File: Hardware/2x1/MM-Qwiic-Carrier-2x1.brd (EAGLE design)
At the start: 109.2 x 34.3 mm, 67 parts, among them J15 MICROMOD-2222-C, J2 QWIIC_RIGHT_ANGLE, U1 MCP73831, U5 AP7361C-33FGEUDFN-8

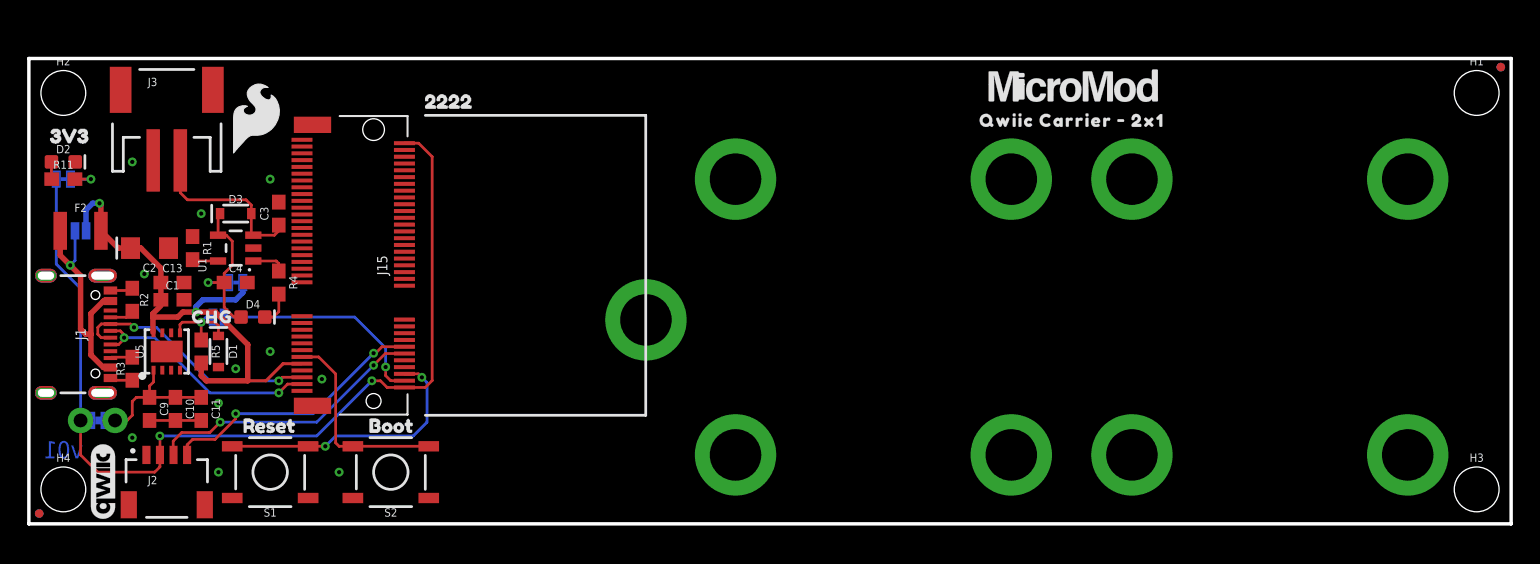
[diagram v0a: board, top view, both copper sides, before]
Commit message: Fix silk screen
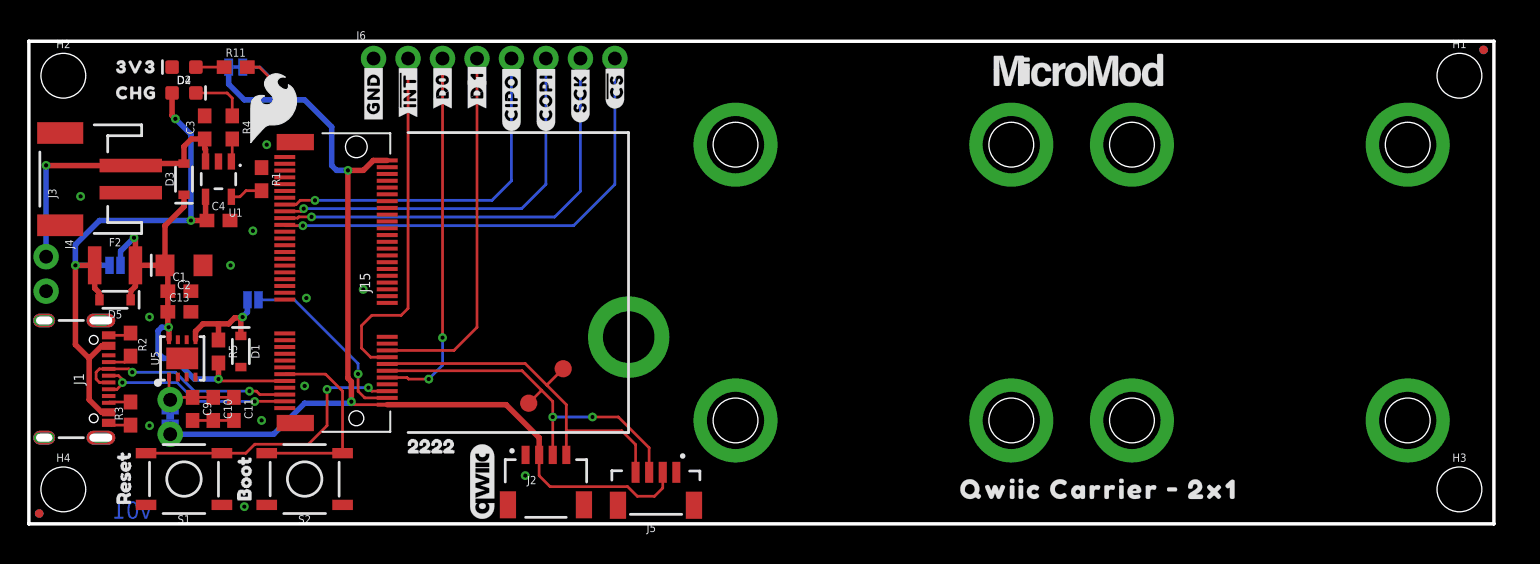
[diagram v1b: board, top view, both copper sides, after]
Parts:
- removed H10, H11, H12, H13, H6, H7, H8, H9: STAND-OFF-REFLOW2.5MM_TALL, SparkFun-Hardware:STAND-OFF-REFLOW-M2.5
- removed JP1: JUMPER-SMT_2_NC_TRACE_SILK, SparkFun-Jumpers:SMT-JUMPER_2_NC_TRACE_SILK
- removed U$10: (no value), output:QWIIC_CARRIER_#_2X10
- added D5: 3A/10V/280mV, SparkFun-DiscreteSemi:SOD-323
- added J4: (no value), SparkFun-Connectors:1X02_NO_SILK
- added J5: Vertical Qwiic Connector, SparkFun-Connectors:JST04_1MM_VERT
- added J6: (no value), SparkFun-Connectors:1X08_NO_SILK
- added TP1, TP2: TEST-POINT3X5, SparkFun-Connectors:PAD.03X.05
- added U$11, U$12: (no value), output:QWIIC_CARRIER_#_2X10
- added U$14: (no value), output:#GND#0
- added U$15, U$16: (no value), output:##INT##0
- added U$17, U$18: (no value), output:#D0#0
- added U$20, U$21: (no value), output:#D#0
- added U$22, U$23: (no value), output:#CIPO#0
- added U$24, U$25: (no value), output:#COPI#0
- added U$26, U$27: (no value), output:#SCK#0
- added U$28, U$29: (no value), output:##CS##0
- added U$3: (no value), output:3V30
- added U$30, U$31: (no value), output:#1#0
- added U$32: QWIIC_BOARD_OUTLINESTANDOFF, SparkFun-Boards:QWIIC_BOARD_MOUNT_SMD_STANDOFFS
- U$1: device buzzard_labels (5):3V31 -> output:#3#3V_EN#0
- U$5: value (none) -> QWIIC_BOARD_OUTLINESTANDOFF; device output:#VIN#0 -> SparkFun-Boards:QWIIC_BOARD_MOUNT_SMD_STANDOFFS
- U$8: device output:#VE#0 -> output:#GND#0
- moved U$5 47.9 mm to (62.2, 17.8), flipped to the top
- moved LOGO2 27.9 mm to (33.4, 3.11)
- moved J2 27.9 mm to (38.1, 5.08)
- moved U$55 25.4 mm to (27.0, 5.72)
- moved U$1 19.3 mm to (15.7, 16.5), flipped to the bottom
- moved U$8 18.7 mm to (25.4, 29.5), flipped to the top, turned to 90 degrees
- moved U$4 17.4 mm to (5.71, 31.8)
- moved D4 17.3 mm to (11.4, 31.8)
- moved JP4 15.1 mm to (15.2, 33.7)
- moved R11 15.1 mm to (15.2, 33.7)
- moved U$6 15.1 mm to (21.0, 33.5)
- moved R4 11.9 mm to (15.0, 29.2)
- moved D2 11.3 mm to (11.4, 33.7), turned to 180 degrees
- moved U$19 10.5 mm to (15.9, 0.76), turned to 90 degrees
- moved U$2 10.4 mm to (6.99, 0.51), turned to 90 degrees
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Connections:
- removed net 5V: C4.1, D3.C, D4.A, JP1.2, U1.4
- removed net I2C_SCL: J15.14, J2.4
- removed net I2C_SDA: J15.12, J2.3
- removed net N$5: C3.1, D3.A, J3.2, U1.3
- new net D0: J15.10, J6.3
- new net D1: J15.18, J6.4
- new net I2C_!INT!: J15.16, J6.2
- new net SCL: J15.14, J2.4, J5.4, TP2.P$1
- new net SDA: J15.12, J2.3, J5.3, TP1.P$1
- new net SPI_!CS!: J15.55, J6.8
- new net SPI_CIPO: J15.61, J6.5
- new net SPI_COPI: J15.59, J6.6
- new net SPI_SCK: J15.57, J6.7
- new net V_BATT: C3.1, D3.A, J3.2, J4.1, U1.3
- net 3.3V: now also J5.2
- net GND: now also J4.2, J5.1, J6.1; no longer H10.1, H11.1, H12.1, H13.1, H6.1, H7.1, H8.1, H9.1
- net N$3: now also D4.C; no longer U1.1
- net N$8: now also U1.1; no longer D4.C
- net VIN: now also D3.C, D5.C; no longer JP1.1
- net V_USB: now also C4.1, D4.A, D5.A, U1.4
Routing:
- net SPI_!CS!: track 0.00 -> 34.9 mm, vias 0 -> 1
- net SPI_SCK: track 0.00 -> 32.4 mm, vias 0 -> 1
- net SPI_COPI: track 0.00 -> 29.3 mm, vias 0 -> 1
- net SDA: track 0.00 -> 28.3 mm, vias 0 -> 2
- net SCL: track 0.00 -> 27.4 mm
- net D0: track 0.00 -> 27.1 mm, vias 0 -> 2
- net D1: track 0.00 -> 27.1 mm
- net SPI_CIPO: track 0.00 -> 26.4 mm, vias 0 -> 1
- net I2C_!INT!: track 0.00 -> 26.2 mm
- net V_USB: track 18.2 -> 44.3 mm, vias 1 -> 3
- net V_BATT: track 0.00 -> 21.7 mm, vias 0 -> 1
- net I2C_SDA: track 20.7 -> 0.00 mm, vias 2 -> 0
- net I2C_SCL: track 20.0 -> 0.00 mm, vias 2 -> 0
- net N$5: track 12.7 -> 0.00 mm
- net 5V: track 12.2 -> 0.00 mm, vias 1 -> 0
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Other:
- board size 109.2 x 34.3 mm -> 108 x 35.6 mm
- board text added: "in"

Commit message: silkscreen
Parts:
- added U$33: (no value), output:#GND#0
- added U$34: QWIIC_BOARD_OUTLINESTANDOFF, SparkFun-Boards:QWIIC_BOARD_MOUNT_SMD_STANDOFFS
- added U$35, U$38: (no value), output:QWIIC_CARRIER_#_2X10
- added U$36, U$37: (no value), buzzard_labels (1):#0
- U$11: device output:QWIIC_CARRIER_#_2X10 -> output:#0
- U$12: device output:QWIIC_CARRIER_#_2X10 -> output:#VBAT#0
- U$32: value QWIIC_BOARD_OUTLINESTANDOFF -> (none); device SparkFun-Boards:QWIIC_BOARD_MOUNT_SMD_STANDOFFS -> output:#0
- moved U$32 84.3 mm to (7.75, 27.8)
- moved U$11 68.2 mm to (1.52, 19.7)
- moved U$12 35.4 mm to (7.37, 19.7)
- moved U$67 15.2 mm to (62.1, 33.4)
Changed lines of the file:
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@@
 <?xml version="1.0" encoding="utf-8"?>
 <!DOCTYPE eagle SYSTEM "eagle.dtd">
-<eagle version="9.5.2">
+<eagle version="9.6.2">
 <drawing>
 <settings>
@@
 <wire x1="44.185" y1="6.731" x2="27.94" y2="6.731" width="0.2032" layer="21"/>
 <text x="36.83" y="-21.59" size="1.778" layer="51" font="vector" ratio="15">Priyanka Makin</text>
-<text x="57.404" y="39.878" size="1.778" layer="47" font="vector" ratio="15">in</text>
-<text x="109.474" y="24.511" size="1.778" layer="47" font="vector" ratio="15" rot="R270">in</text>
-<dimension x1="0" y1="35.56" x2="107.95" y2="35.56" x3="53.975" y3="39.37" textsize="1.778" textratio="15" layer="47" unit="inch"/>
-<dimension x1="107.95" y1="35.56" x2="107.95" y2="1.27" x3="111.76" y3="18.415" textsize="1.778" textratio="15" layer="47" unit="inch"/>
+<dimension x1="0" y1="35.56" x2="80.01" y2="35.56" x3="40.005" y3="39.37" textsize="1.778" textratio="15" layer="47" unit="inch"/>
+<dimension x1="80.01" y1="35.56" x2="80.01" y2="0" x3="83.82" y3="17.78" textsize="1.778" textratio="15" layer="47" unit="inch"/>
+<text x="43.434" y="39.878" size="1.778" layer="47" font="vector" ratio="15">in</text>
+<text x="81.534" y="23.241" size="1.778" layer="47" font="vector" ratio="15" rot="R270">in</text>
+<dimension x1="2.54" y1="33.02" x2="77.47" y2="33.02" x3="40.005" y3="44.45" textsize="1.778" textratio="15" layer="47" unit="inch"/>
+<dimension x1="77.47" y1="33.02" x2="77.47" y2="2.54" x3="88.9" y3="17.78" textsize="1.778" textratio="15" layer="47" unit="inch"/>
+<text x="43.434" y="44.958" size="1.778" layer="47" font="vector" ratio="15">in</text>
+<text x="86.614" y="23.241" size="1.778" layer="47" font="vector" ratio="15" rot="R270">in</text>
 </plain>
 <attributes>
@@
 <element name="LOGO1" library="SparkFun-Aesthetics" package="SFE_LOGO_NAME_FLAME_.2" value="SFE_LOGO_NAME_FLAME.2_INCH" x="31.75" y="21.59" smashed="yes" rot="MR0"/>
 <element name="U$44" library="SparkFun-Aesthetics" package="SFE_LOGO_FLAME_.2" value="" x="18.034" y="30.607" smashed="yes"/>
-<element name="U$67" library="SparkFun-MicroMod" package="MICROMOD_LOGO_.5" value="" x="77.343" y="33.401" smashed="yes"/>
+<element name="U$67" library="SparkFun-MicroMod" package="MICROMOD_LOGO_.5" value="" x="62.103" y="33.401" smashed="yes"/>
 <element name="U$68" library="SparkFun-MicroMod" package="MICROMOD_LOGO_.5" value="" x="31.75" y="19.05" smashed="yes" rot="MR0"/>
 <element name="J2" library="SparkFun-Connectors" package="JST04_1MM_RA" value="QWIIC_RIGHT_ANGLE" x="38.1" y="5.08" smashed="yes">
@@
 </element>
 <element name="U$5" library="SparkFun-Boards" package="QWIIC_BOARD_MOUNT_SMD_STANDOFFS" value="QWIIC_BOARD_OUTLINESTANDOFF" x="62.23" y="17.78" smashed="yes"/>
-<element name="U$11" library="output" package="QWIIC_CARRIER_#_2X10" value="" x="67.564" y="2.54" smashed="yes"/>
-<element name="U$12" library="output" package="QWIIC_CARRIER_#_2X10" value="" x="42.672" y="16.51" smashed="yes" rot="MR0"/>
 <element name="U$3" library="output" package="3V30" value="" x="5.715" y="33.655" smashed="yes"/>
 <element name="U$1" library="output" package="#3#3V_EN#0" value="" x="15.748" y="16.51" smashed="yes" rot="MR0"/>
@@
 <element name="U$30" library="output" package="#1#0" value="" x="33.02" y="32.004" smashed="yes" rot="R90"/>
 <element name="U$31" library="output" package="#1#0" value="" x="33.02" y="32.004" smashed="yes" rot="MR90"/>
-<element name="U$32" library="SparkFun-Boards" package="QWIIC_BOARD_MOUNT_SMD_STANDOFFS" value="QWIIC_BOARD_OUTLINESTANDOFF" x="91.44" y="17.78" smashed="yes"/>
+<element name="U$12" library="output" package="#VBAT#0" value="" x="7.366" y="19.685" smashed="yes" rot="MR0"/>
+<element name="U$33" library="output" package="#GND#0" value="" x="6.096" y="17.145" smashed="yes" rot="MR0"/>
+<element name="U$11" library="output" package="#0" value="" x="1.524" y="19.685" smashed="yes"/>
+<element name="U$32" library="output" package="#0" value="" x="7.747" y="27.813" smashed="yes"/>
+<element name="U$36" library="buzzard_labels (1)" package="#0" value="" x="1.143" y="17.399" smashed="yes"/>
+<element name="U$37" library="buzzard_labels (1)" package="#0" value="" x="7.366" y="23.495" smashed="yes"/>
+<element name="U$34" library="SparkFun-Boards" package="QWIIC_BOARD_MOUNT_SMD_STANDOFFS" value="QWIIC_BOARD_OUTLINESTANDOFF" x="91.44" y="17.78" smashed="yes"/>
+<element name="U$35" library="output" package="QWIIC_CARRIER_#_2X10" value="" x="51.054" y="2.54" smashed="yes"/>
+<element name="U$38" library="output" package="QWIIC_CARRIER_#_2X10" value="" x="42.926" y="16.764" smashed="yes" rot="MR0"/>
 </elements>
 <signals>

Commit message: Update MM-Qwiic-Carrier-2x1.brd
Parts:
- moved U$67 15.2 mm to (77.3, 33.4)
- moved U$35 14.0 mm to (65.0, 2.54)
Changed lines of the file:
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@@
 <?xml version="1.0" encoding="utf-8"?>
 <!DOCTYPE eagle SYSTEM "eagle.dtd">
-<eagle version="9.6.2">
+<eagle version="9.5.2">
 <drawing>
 <settings>
@@
 <wire x1="44.185" y1="6.731" x2="27.94" y2="6.731" width="0.2032" layer="21"/>
 <text x="36.83" y="-21.59" size="1.778" layer="51" font="vector" ratio="15">Priyanka Makin</text>
-<dimension x1="0" y1="35.56" x2="80.01" y2="35.56" x3="40.005" y3="39.37" textsize="1.778" textratio="15" layer="47" unit="inch"/>
-<dimension x1="80.01" y1="35.56" x2="80.01" y2="0" x3="83.82" y3="17.78" textsize="1.778" textratio="15" layer="47" unit="inch"/>
-<text x="43.434" y="39.878" size="1.778" layer="47" font="vector" ratio="15">in</text>
-<text x="81.534" y="23.241" size="1.778" layer="47" font="vector" ratio="15" rot="R270">in</text>
-<dimension x1="2.54" y1="33.02" x2="77.47" y2="33.02" x3="40.005" y3="44.45" textsize="1.778" textratio="15" layer="47" unit="inch"/>
-<dimension x1="77.47" y1="33.02" x2="77.47" y2="2.54" x3="88.9" y3="17.78" textsize="1.778" textratio="15" layer="47" unit="inch"/>
-<text x="43.434" y="44.958" size="1.778" layer="47" font="vector" ratio="15">in</text>
-<text x="86.614" y="23.241" size="1.778" layer="47" font="vector" ratio="15" rot="R270">in</text>
+<text x="57.404" y="39.878" size="1.778" layer="47" font="vector" ratio="15">in</text>
+<text x="110.744" y="23.241" size="1.778" layer="47" font="vector" ratio="15" rot="R270">in</text>
+<text x="57.404" y="43.688" size="1.778" layer="47" font="vector" ratio="15">in</text>
+<text x="114.554" y="23.241" size="1.778" layer="47" font="vector" ratio="15" rot="R270">in</text>
+<dimension x1="0" y1="35.56" x2="107.95" y2="35.56" x3="53.975" y3="43.18" textsize="1.778" textratio="15" layer="47" unit="inch"/>
+<dimension x1="2.54" y1="33.02" x2="105.41" y2="33.02" x3="53.975" y3="39.37" textsize="1.778" textratio="15" layer="47" unit="inch"/>
+<dimension x1="105.41" y1="33.02" x2="105.41" y2="2.54" x3="113.03" y3="17.78" textsize="1.778" textratio="15" layer="47" unit="inch"/>
+<dimension x1="107.95" y1="35.56" x2="107.95" y2="0" x3="116.84" y3="17.78" textsize="1.778" textratio="15" layer="47" unit="inch"/>
 </plain>
 <attributes>
@@
 <element name="LOGO1" library="SparkFun-Aesthetics" package="SFE_LOGO_NAME_FLAME_.2" value="SFE_LOGO_NAME_FLAME.2_INCH" x="31.75" y="21.59" smashed="yes" rot="MR0"/>
 <element name="U$44" library="SparkFun-Aesthetics" package="SFE_LOGO_FLAME_.2" value="" x="18.034" y="30.607" smashed="yes"/>
-<element name="U$67" library="SparkFun-MicroMod" package="MICROMOD_LOGO_.5" value="" x="62.103" y="33.401" smashed="yes"/>
+<element name="U$67" library="SparkFun-MicroMod" package="MICROMOD_LOGO_.5" value="" x="77.343" y="33.401" smashed="yes"/>
 <element name="U$68" library="SparkFun-MicroMod" package="MICROMOD_LOGO_.5" value="" x="31.75" y="19.05" smashed="yes" rot="MR0"/>
 <element name="J2" library="SparkFun-Connectors" package="JST04_1MM_RA" value="QWIIC_RIGHT_ANGLE" x="38.1" y="5.08" smashed="yes">
@@
 <element name="U$37" library="buzzard_labels (1)" package="#0" value="" x="7.366" y="23.495" smashed="yes"/>
 <element name="U$34" library="SparkFun-Boards" package="QWIIC_BOARD_MOUNT_SMD_STANDOFFS" value="QWIIC_BOARD_OUTLINESTANDOFF" x="91.44" y="17.78" smashed="yes"/>
-<element name="U$35" library="output" package="QWIIC_CARRIER_#_2X10" value="" x="51.054" y="2.54" smashed="yes"/>
+<element name="U$35" library="output" package="QWIIC_CARRIER_#_2X10" value="" x="65.024" y="2.54" smashed="yes"/>
 <element name="U$38" library="output" package="QWIIC_CARRIER_#_2X10" value="" x="42.926" y="16.764" smashed="yes" rot="MR0"/>
 </elements>

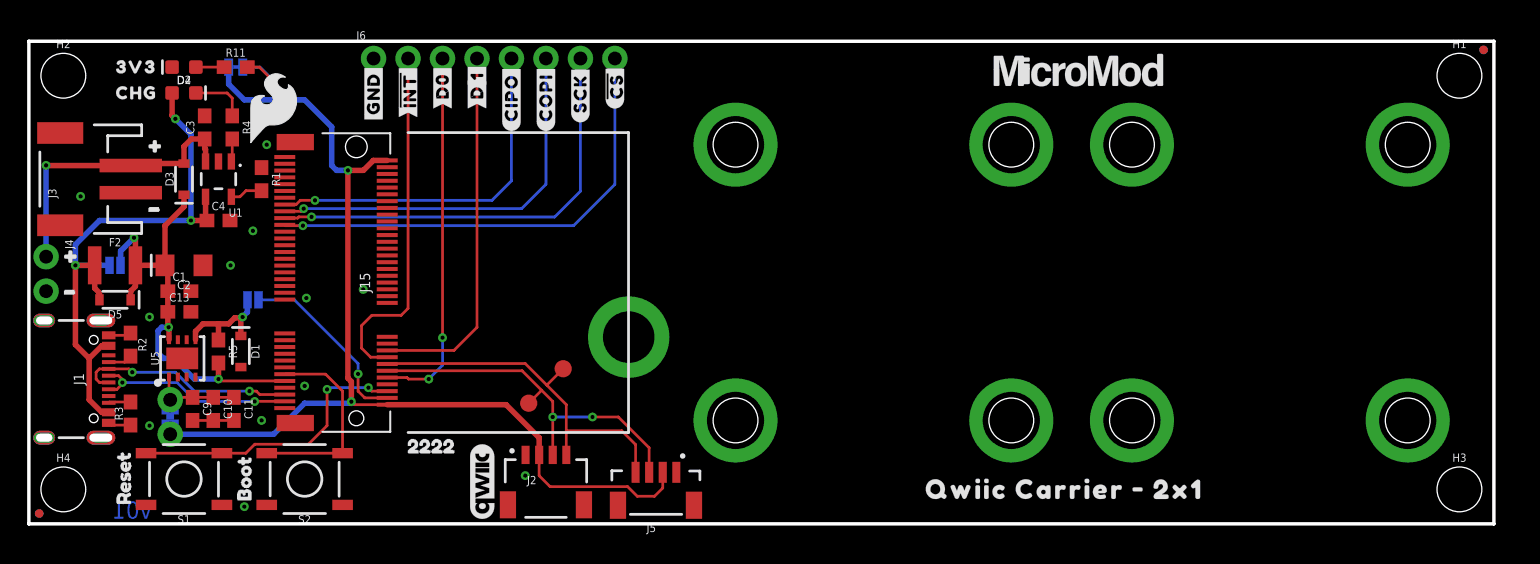
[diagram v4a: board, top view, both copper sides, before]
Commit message: silk screen
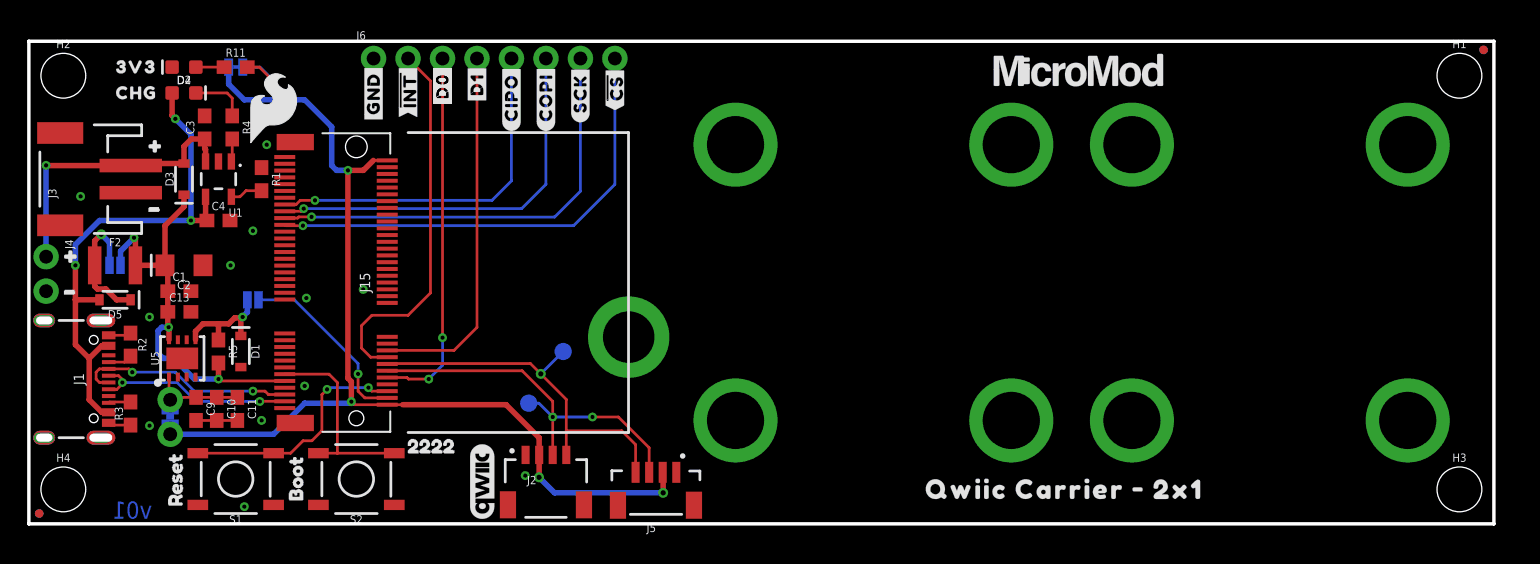
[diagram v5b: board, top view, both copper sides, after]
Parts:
- removed U$35, U$38: (no value), output:QWIIC_CARRIER_#_2X10
- U$20, U$21: device output:#D#0 -> output:#D1#0
- U$30: value (none) -> QWIIC_BOARD_OUTLINESTANDOFF; device output:#1#0 -> SparkFun-Boards:QWIIC_BOARD_MOUNT_SMD_STANDOFFS
- U$31: device output:#1#0 -> output:QWIIC_CARRIER_#_2X10
- U$34: value QWIIC_BOARD_OUTLINESTANDOFF -> (none); device SparkFun-Boards:QWIIC_BOARD_MOUNT_SMD_STANDOFFS -> output:QWIIC_CARRIER_#_2X10
- moved U$30 60.1 mm to (91.4, 17.8), turned to 0 degrees
- moved U$34 48.5 mm to (42.9, 16.8), flipped to the bottom
- moved U$31 43.5 mm to (65.0, 2.54), flipped to the top, turned to 0 degrees
- moved U$2 3.81 mm to (10.8, 0.38)
- moved S1 3.81 mm to (15.2, 3.30)
- moved S2 3.81 mm to (24.1, 3.30)
- moved U$19 3.81 mm to (19.7, 0.76)
- moved TP2 1.27 mm to (39.4, 12.7), flipped to the bottom
- moved C11 0.25 mm to (15.4, 8.47)
- moved C9 0.25 mm to (12.3, 8.47)
- moved U$20 0.25 mm to (33.0, 30.9)
- moved U$21 0.25 mm to (33.0, 30.9)
- moved C10 0.25 mm to (13.8, 8.47)
- moved U$28 0.13 mm to (43.2, 30.5)
- moved U$29 0.13 mm to (43.2, 30.5)
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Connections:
- new net V_USB_2: BYP.1, D5.C, F2.1
- net VIN: no longer D5.C
- net V_USB: no longer BYP.1, F2.1
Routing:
- net V_USB_2: track 0.00 -> 9.63 mm, vias 0 -> 1
- net V_USB: track 44.3 -> 39.5 mm
- net !RESET!: track 21.4 -> 17.6 mm
- net VIN: track 34.7 -> 32.0 mm
- net I2C_!INT!: track 26.2 -> 27.9 mm
- net SCL: track 27.4 -> 28.3 mm, vias 0 -> 1
- net SDA: track 28.3 -> 29.1 mm
- net 3.3V: track 78.7 -> 78.8 mm, vias 2 -> 4
